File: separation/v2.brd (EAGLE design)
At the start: 0 parts

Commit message: add mcu
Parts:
- added JP2, JP4: (no value), microbuilder:1X07_OVAL
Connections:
- new net +3V3: JP4.5
- new net A0: JP2.1
- new net A1: JP2.2
- new net A2: JP2.3
- new net A3: JP2.4
- new net GND: JP4.6
- new net MISO: JP4.3
- new net MOSI: JP4.4
- new net RX: JP4.1
- new net SCK: JP4.2
- new net SCL: JP2.6
- new net SDA: JP2.5
- new net TX: JP2.7
- new net VCC: JP4.7
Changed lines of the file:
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@@
 <layer number="23" name="tOrigins" color="15" fill="1" visible="yes" active="yes"/>
 <layer number="24" name="bOrigins" color="15" fill="1" visible="yes" active="yes"/>
-<layer number="25" name="tNames" color="7" fill="1" visible="no" active="yes"/>
+<layer number="25" name="tNames" color="7" fill="1" visible="yes" active="yes"/>
 <layer number="26" name="bNames" color="7" fill="1" visible="no" active="yes"/>
 <layer number="27" name="tValues" color="7" fill="1" visible="no" active="yes"/>
 <layer number="28" name="bValues" color="7" fill="1" visible="no" active="yes"/>
-<layer number="29" name="tStop" color="7" fill="3" visible="no" active="yes"/>
+<layer number="29" name="tStop" color="7" fill="3" visible="yes" active="yes"/>
 <layer number="30" name="bStop" color="7" fill="6" visible="no" active="yes"/>
 <layer number="31" name="tCream" color="7" fill="4" visible="no" active="yes"/>
@@
 <wire x1="30.48" y1="64.897" x2="32.258" y2="64.897" width="1.524" layer="29"/>
 <circle x="0" y="0" radius="38" width="0.254" layer="49"/>
+<wire x1="8.89" y1="32.131" x2="8.89" y2="16.51" width="0.254" layer="21"/>
+<wire x1="8.89" y1="16.51" x2="6.35" y2="13.97" width="0.254" layer="21" curve="-90"/>
+<wire x1="6.35" y1="13.97" x2="-6.35" y2="13.97" width="0.254" layer="21"/>
+<wire x1="-6.35" y1="13.97" x2="-8.89" y2="16.51" width="0.254" layer="21" curve="-90"/>
+<wire x1="-8.89" y1="16.51" x2="-8.89" y2="32.131" width="0.254" layer="21"/>
+<wire x1="-8.89" y1="32.131" x2="-6.35" y2="34.671" width="0.254" layer="21" curve="-90"/>
+<wire x1="-6.35" y1="34.671" x2="6.35" y2="34.671" width="0.254" layer="21"/>
+<wire x1="6.35" y1="34.671" x2="8.89" y2="32.131" width="0.254" layer="21" curve="-90"/>
+<text x="64.4398" y="16.5608" size="1.016" layer="21" font="vector" ratio="12" rot="R180" align="center"></text>
+<wire x1="-7.62" y1="32.004" x2="-9.525" y2="32.004" width="1.524" layer="29"/>
+<wire x1="-7.62" y1="29.337" x2="-9.398" y2="29.337" width="1.524" layer="29"/>
+<wire x1="-7.62" y1="26.797" x2="-7.747" y2="26.924" width="1.524" layer="29"/>
+<wire x1="-7.62" y1="21.844" x2="-7.747" y2="21.717" width="1.524" layer="29"/>
+<wire x1="-7.747" y1="21.717" x2="-9.398" y2="21.717" width="1.524" layer="29"/>
+<wire x1="-7.62" y1="26.797" x2="-9.398" y2="26.797" width="1.524" layer="29"/>
+<wire x1="-7.62" y1="24.257" x2="-9.398" y2="24.257" width="1.524" layer="29"/>
+<wire x1="-7.62" y1="19.177" x2="-9.398" y2="19.177" width="1.524" layer="29"/>
+<wire x1="-7.62" y1="16.637" x2="-9.398" y2="16.637" width="1.524" layer="29"/>
+<wire x1="7.62" y1="31.877" x2="9.398" y2="31.877" width="1.524" layer="29"/>
+<wire x1="7.62" y1="29.337" x2="9.398" y2="29.337" width="1.524" layer="29"/>
+<wire x1="7.62" y1="26.797" x2="9.398" y2="26.797" width="1.524" layer="29"/>
+<wire x1="7.62" y1="24.257" x2="9.398" y2="24.257" width="1.524" layer="29"/>
+<wire x1="7.62" y1="21.717" x2="9.398" y2="21.717" width="1.524" layer="29"/>
+<wire x1="7.62" y1="19.177" x2="9.398" y2="19.177" width="1.524" layer="29"/>
+<wire x1="7.62" y1="16.637" x2="9.398" y2="16.637" width="1.524" layer="29"/>
 </plain>
 <attributes>
@@
 </autorouter>
 <elements>
+<element name="JP2" library="microbuilder" package="1X07_OVAL" value="" x="-7.62" y="24.3205" smashed="yes" rot="R270">
+<attribute name="NAME" x="-5.7912" y="33.2867" size="0.8128" layer="25" ratio="18" rot="R270"/>
+<attribute name="VALUE" x="-10.795" y="33.2105" size="0.4064" layer="27" ratio="10" rot="R270"/>
+</element>
+<element name="JP4" library="microbuilder" package="1X07_OVAL" value="" x="7.62" y="24.3205" smashed="yes" rot="R90">
+<attribute name="NAME" x="5.7912" y="15.3543" size="0.8128" layer="25" ratio="18" rot="R90"/>
+<attribute name="VALUE" x="10.795" y="15.4305" size="0.4064" layer="27" ratio="10" rot="R90"/>
+</element>
 </elements>
 <signals>
@@
 <signal name="PB03/I3/AIN11/SERCOM5.2">
 </signal>
+<signal name="GND" class="1">
+<contactref element="JP4" pad="6"/>
+</signal>
+<signal name="A0">
+<contactref element="JP2" pad="1"/>
+</signal>
+<signal name="A1">
+<contactref element="JP2" pad="2"/>
+</signal>
+<signal name="MOSI">
+<contactref element="JP4" pad="4"/>
+</signal>
+<signal name="MISO">
+<contactref element="JP4" pad="3"/>
+</signal>
+<signal name="SCK">
+<contactref element="JP4" pad="2"/>
+</signal>
+<signal name="A2">
+<contactref element="JP2" pad="3"/>
+</signal>
+<signal name="A3">
+<contactref element="JP2" pad="4"/>
+</signal>
+<signal name="SDA">
+<contactref element="JP2" pad="5"/>
+</signal>
+<signal name="SCL">
+<contactref element="JP2" pad="6"/>
+</signal>
+<signal name="VCC" class="1">
+<contactref element="JP4" pad="7"/>
+</signal>
+<signal name="+3V3">
+<contactref element="JP4" pad="5"/>
+</signal>
+<signal name="PB22/I6/SERCOM5.3">
+</signal>
+<signal name="PB23/I7/SERCOM5.2">
+</signal>
+<signal name="PB03/I3/AIN11/SERCOM5.3">
+</signal>
+<signal name="TX">
+<contactref element="JP2" pad="7"/>
+</signal>
+<signal name="RX">
+<contactref element="JP4" pad="1"/>
+</signal>
 </signals>

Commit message: 9mm buzzer
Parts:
- added LS1: KSTG931AP, SamacSys_Parts:CAPPRD400W70D900H500
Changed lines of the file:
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@@
 <attribute name="VALUE" x="10.795" y="15.4305" size="0.4064" layer="27" ratio="10" rot="R90"/>
+</element>
+<element name="LS1" library="SamacSys_Parts" package="CAPPRD400W70D900H500" package3d_urn="urn:adsk.eagle:package:34276129/2" value="KSTG931AP" x="-33.02" y="-43.18" smashed="yes">
+<attribute name="DESCRIPTION" value="RS PRO 4V Electromagnetic Buzzer, 92dB" x="-33.02" y="-43.18" size="1.778" layer="27" font="vector" ratio="15" display="off"/>
+<attribute name="HEIGHT" value="5mm" x="-33.02" y="-43.18" size="1.778" layer="27" font="vector" ratio="15" display="off"/>
+<attribute name="MANUFACTURER_NAME" value="RS Components" x="-33.02" y="-43.18" size="1.778" layer="27" font="vector" ratio="15" display="off"/>
+<attribute name="MANUFACTURER_PART_NUMBER" value="KSTG931AP" x="-33.02" y="-43.18" size="1.778" layer="27" font="vector" ratio="15" display="off"/>
+<attribute name="NAME" x="-33.02" y="-43.18" size="1.27" layer="25" align="center"/>
+<attribute name="RS_PART_NUMBER" value="" x="-33.02" y="-43.18" size="1.778" layer="27" font="vector" ratio="15" display="off"/>
+<attribute name="RS_PRICE-STOCK" value="" x="-33.02" y="-43.18" size="1.778" layer="27" font="vector" ratio="15" display="off"/>
+<attribute name="VALUE" x="-33.02" y="-43.18" size="1.27" layer="27" align="center"/>
 </element>
 </elements>
@@
 </board>
 </drawing>
+<compatibility>
+<note version="8.3" severity="warning">
+Since Version 8.3, EAGLE supports URNs for individual library
+assets (packages, symbols, and devices). The URNs of those assets
+will not be understood (or retained) with this version.
+</note>
+<note version="8.3" severity="warning">
+Since Version 8.3, EAGLE supports the association of 3D packages
+with devices in libraries, schematics, and board files. Those 3D
+packages will not be understood (or retained) with this version.
+</note>
+</compatibility>
 </eagle>

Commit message: add support components
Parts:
- added BAT: MB332-350M02SZ, SamacSys_Parts:MB332350M02SZ
- added LDO: L7805ACV, SamacSys_Parts:TO255P460X1020X2008-3P
- renumbered LS1 to LOUD
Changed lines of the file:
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@@
 <attribute name="VALUE" x="10.795" y="15.4305" size="0.4064" layer="27" ratio="10" rot="R90"/>
 </element>
-<element name="LS1" library="SamacSys_Parts" package="CAPPRD400W70D900H500" package3d_urn="urn:adsk.eagle:package:34276129/2" value="KSTG931AP" x="-33.02" y="-43.18" smashed="yes">
+<element name="LOUD" library="SamacSys_Parts" package="CAPPRD400W70D900H500" package3d_urn="urn:adsk.eagle:package:34276129/2" value="KSTG931AP" x="-33.02" y="-43.18" smashed="yes">
 <attribute name="DESCRIPTION" value="RS PRO 4V Electromagnetic Buzzer, 92dB" x="-33.02" y="-43.18" size="1.778" layer="27" font="vector" ratio="15" display="off"/>
 <attribute name="HEIGHT" value="5mm" x="-33.02" y="-43.18" size="1.778" layer="27" font="vector" ratio="15" display="off"/>
@@
 <attribute name="VALUE" x="-33.02" y="-43.18" size="1.27" layer="27" align="center"/>
 </element>
+<element name="LDO" library="SamacSys_Parts" package="TO255P460X1020X2008-3P" package3d_urn="urn:adsk.eagle:package:34276127/2" value="L7805ACV" x="-34.29" y="-52.07" smashed="yes">
+<attribute name="ALLIED_NUMBER" value="70013701" x="-34.29" y="-52.07" size="1.778" layer="27" font="vector" ratio="15" display="off"/>
+<attribute name="DESCRIPTION" value="Linear voltage regulator,L7805ACV 5V 1A STMicroelectronics L7805ACV, Single Linear Voltage Regulator, 1A 5 V, 2%, 3-Pin TO-220" x="-34.29" y="-52.07" size="1.778" layer="27" font="vector" ratio="15" display="off"/>
+<attribute name="HEIGHT" value="4.6mm" x="-34.29" y="-52.07" size="1.778" layer="27" font="vector" ratio="15" display="off"/>
+<attribute name="MANUFACTURER_NAME" value="STMicroelectronics" x="-34.29" y="-52.07" size="1.778" layer="27" font="vector" ratio="15" display="off"/>
+<attribute name="MANUFACTURER_PART_NUMBER" value="L7805ACV" x="-34.29" y="-52.07" size="1.778" layer="27" font="vector" ratio="15" display="off"/>
+<attribute name="NAME" x="-34.29" y="-52.07" size="1.27" layer="25" align="center"/>
+<attribute name="RS_PART_NUMBER" value="2988508P" x="-34.29" y="-52.07" size="1.778" layer="27" font="vector" ratio="15" display="off"/>
+<attribute name="RS_PRICE-STOCK" value="http://uk.rs-online.com/web/p/products/2988508P" x="-34.29" y="-52.07" size="1.778" layer="27" font="vector" ratio="15" display="off"/>
+<attribute name="VALUE" x="-34.29" y="-52.07" size="1.27" layer="27" align="center"/>
+</element>
+<element name="BAT" library="SamacSys_Parts" package="MB332350M02SZ" value="MB332-350M02SZ" x="-45.72" y="-48.26" smashed="yes">
+<attribute name="DESCRIPTION" value="RS PRO 3.5mm Pitch Straight, PCB Terminal Block, Through Hole, 2 Way" x="-45.72" y="-48.26" size="1.778" layer="27" font="vector" ratio="15" display="off"/>
+<attribute name="HEIGHT" value="12.76mm" x="-45.72" y="-48.26" size="1.778" layer="27" font="vector" ratio="15" display="off"/>
+<attribute name="MANUFACTURER_NAME" value="RS Components" x="-45.72" y="-48.26" size="1.778" layer="27" font="vector" ratio="15" display="off"/>
+<attribute name="MANUFACTURER_PART_NUMBER" value="MB332-350M02SZ" x="-45.72" y="-48.26" size="1.778" layer="27" font="vector" ratio="15" display="off"/>
+<attribute name="NAME" x="-43.97" y="-48.36" size="1.27" layer="25" align="center"/>
+<attribute name="RS_PART_NUMBER" value="7901149" x="-45.72" y="-48.26" size="1.778" layer="27" font="vector" ratio="15" display="off"/>
+<attribute name="RS_PRICE-STOCK" value="https://uk.rs-online.com/web/p/products/7901149" x="-45.72" y="-48.26" size="1.778" layer="27" font="vector" ratio="15" display="off"/>
+<attribute name="VALUE" x="-43.97" y="-48.36" size="1.27" layer="27" align="center"/>
+</element>
 </elements>

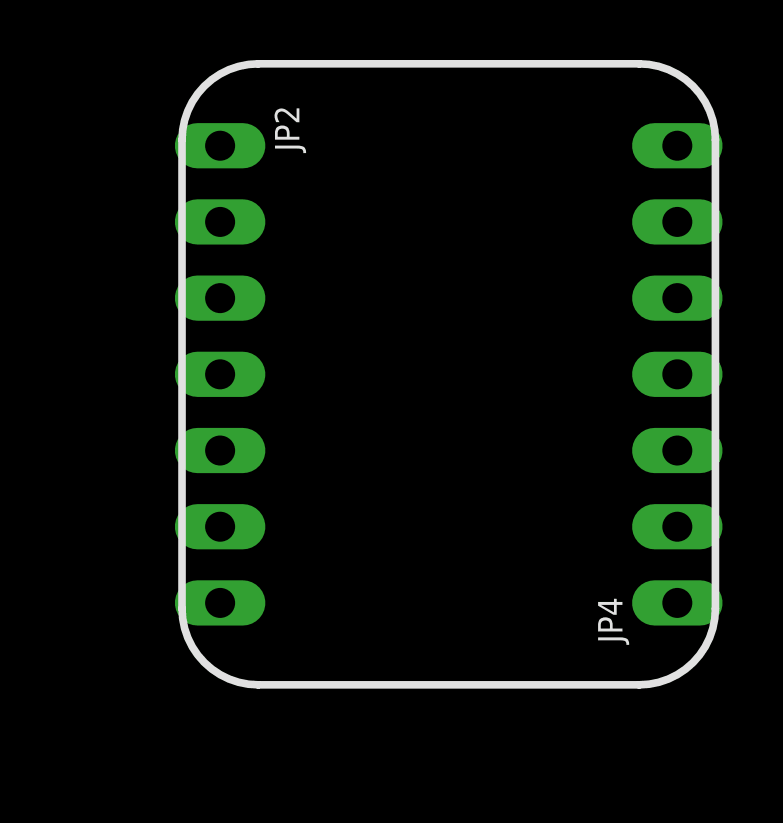
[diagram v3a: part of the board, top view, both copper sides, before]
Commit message: rename components to be helpful
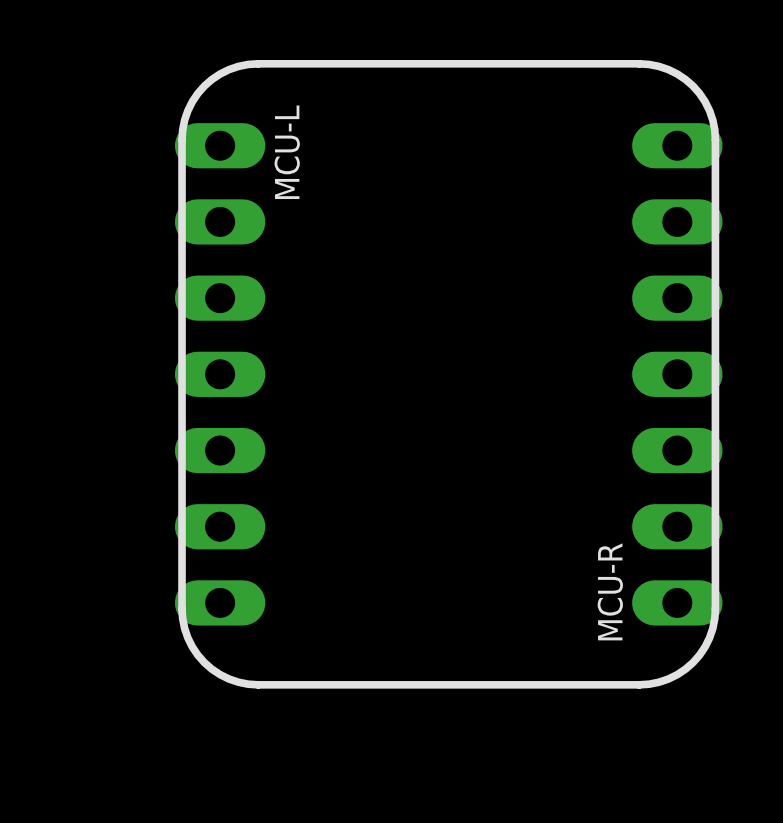
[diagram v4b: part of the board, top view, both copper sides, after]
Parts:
- renumbered JP2 to MCU-L, JP4 to MCU-R
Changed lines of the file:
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@@
 </autorouter>
 <elements>
-<element name="JP2" library="microbuilder" package="1X07_OVAL" value="" x="-7.62" y="24.3205" smashed="yes" rot="R270">
+<element name="MCU-L" library="microbuilder" package="1X07_OVAL" value="" x="-7.62" y="24.3205" smashed="yes" rot="R270">
 <attribute name="NAME" x="-5.7912" y="33.2867" size="0.8128" layer="25" ratio="18" rot="R270"/>
 <attribute name="VALUE" x="-10.795" y="33.2105" size="0.4064" layer="27" ratio="10" rot="R270"/>
 </element>
-<element name="JP4" library="microbuilder" package="1X07_OVAL" value="" x="7.62" y="24.3205" smashed="yes" rot="R90">
+<element name="MCU-R" library="microbuilder" package="1X07_OVAL" value="" x="7.62" y="24.3205" smashed="yes" rot="R90">
 <attribute name="NAME" x="5.7912" y="15.3543" size="0.8128" layer="25" ratio="18" rot="R90"/>
 <attribute name="VALUE" x="10.795" y="15.4305" size="0.4064" layer="27" ratio="10" rot="R90"/>
@@
 </signal>
 <signal name="GND" class="1">
-<contactref element="JP4" pad="6"/>
+<contactref element="MCU-R" pad="6"/>
 </signal>
 <signal name="A0">
-<contactref element="JP2" pad="1"/>
+<contactref element="MCU-L" pad="1"/>
 </signal>
 <signal name="A1">
-<contactref element="JP2" pad="2"/>
+<contactref element="MCU-L" pad="2"/>
 </signal>
 <signal name="MOSI">
-<contactref element="JP4" pad="4"/>
+<contactref element="MCU-R" pad="4"/>
 </signal>
 <signal name="MISO">
-<contactref element="JP4" pad="3"/>
+<contactref element="MCU-R" pad="3"/>
 </signal>
 <signal name="SCK">
-<contactref element="JP4" pad="2"/>
+<contactref element="MCU-R" pad="2"/>
 </signal>
 <signal name="A2">
-<contactref element="JP2" pad="3"/>
+<contactref element="MCU-L" pad="3"/>
 </signal>
 <signal name="A3">
-<contactref element="JP2" pad="4"/>
+<contactref element="MCU-L" pad="4"/>
 </signal>
 <signal name="SDA">
-<contactref element="JP2" pad="5"/>
+<contactref element="MCU-L" pad="5"/>
 </signal>
 <signal name="SCL">
-<contactref element="JP2" pad="6"/>
+<contactref element="MCU-L" pad="6"/>
 </signal>
 <signal name="VCC" class="1">
-<contactref element="JP4" pad="7"/>
+<contactref element="MCU-R" pad="7"/>
 </signal>
 <signal name="+3V3">
-<contactref element="JP4" pad="5"/>
+<contactref element="MCU-R" pad="5"/>
 </signal>
 <signal name="PB22/I6/SERCOM5.3">
@@
 </signal>
 <signal name="TX">
-<contactref element="JP2" pad="7"/>
+<contactref element="MCU-L" pad="7"/>
 </signal>
 <signal name="RX">
-<contactref element="JP4" pad="1"/>
+<contactref element="MCU-R" pad="1"/>
 </signal>
 </signals>

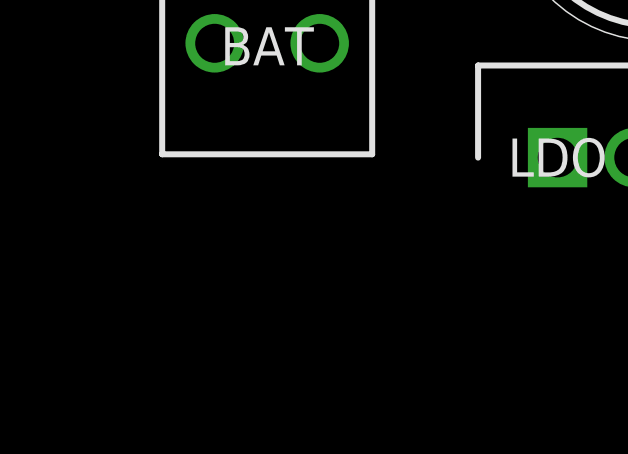
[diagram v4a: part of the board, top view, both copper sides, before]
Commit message: servo connection
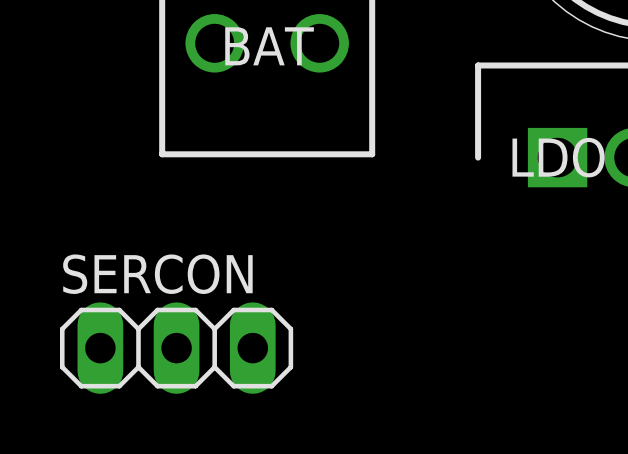
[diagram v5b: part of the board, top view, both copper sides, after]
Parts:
- added SERCON: (no value), pinhead:1X03
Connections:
- new net SERVO: SERCON.3
- new net VBAT: SERCON.1
- net GND: now also SERCON.2
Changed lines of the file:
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@@
 <attribute name="VALUE" x="-43.97" y="-48.36" size="1.27" layer="27" align="center"/>
+</element>
+<element name="SERCON" library="pinhead" library_urn="urn:adsk.eagle:library:325" package="1X03" package3d_urn="urn:adsk.eagle:package:22458/2" value="" x="-46.99" y="-58.42" smashed="yes">
+<attribute name="NAME" x="-50.8762" y="-56.5912" size="1.27" layer="25" ratio="10"/>
+<attribute name="POPULARITY" value="92" x="-46.99" y="-58.42" size="1.778" layer="27" font="vector" ratio="15" display="off"/>
+<attribute name="VALUE" x="-50.8" y="-61.595" size="1.27" layer="27"/>
 </element>
 </elements>
@@
 <signal name="GND" class="1">
 <contactref element="MCU-R" pad="6"/>
+<contactref element="SERCON" pad="2"/>
+<wire x1="7.62" y1="29.4005" x2="-46.99" y2="-58.42" width="0" layer="19" extent="1-1"/>
 </signal>
 <signal name="A0">
@@
 <contactref element="MCU-R" pad="1"/>
 </signal>
+<signal name="VBAT">
+<contactref element="SERCON" pad="1"/>
+</signal>
+<signal name="SERVO">
+<contactref element="SERCON" pad="3"/>
+</signal>
 </signals>
 <mfgpreviewcolors>
@@
 </drawing>
 <compatibility>
+<note version="8.2" severity="warning">
+Since Version 8.2, EAGLE supports online libraries. The ids
+of those online libraries will not be understood (or retained)
+with this version.
+</note>
 <note version="8.3" severity="warning">
 Since Version 8.3, EAGLE supports URNs for individual library

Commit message: ground components
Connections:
- net GND: now also BAT.2, LDO.2, LOUD.2
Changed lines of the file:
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@@
 <contactref element="MCU-R" pad="6"/>
 <contactref element="SERCON" pad="2"/>
-<wire x1="7.62" y1="29.4005" x2="-46.99" y2="-58.42" width="0" layer="19" extent="1-1"/>
+<contactref element="BAT" pad="2"/>
+<contactref element="LDO" pad="2"/>
+<contactref element="LOUD" pad="2"/>
+<wire x1="-42.22" y1="-48.26" x2="-46.99" y2="-58.42" width="0" layer="19" extent="1-1"/>
+<wire x1="-31.74" y1="-52.07" x2="-42.22" y2="-48.26" width="0" layer="19" extent="1-1"/>
+<wire x1="-29.02" y1="-43.18" x2="-31.74" y2="-52.07" width="0" layer="19" extent="1-1"/>
+<wire x1="7.62" y1="29.4005" x2="-29.02" y2="-43.18" width="0" layer="19" extent="1-1"/>
 </signal>
 <signal name="A0">

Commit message: connect components to nets
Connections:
- new net BUZZ: LOUD.1
- net VBAT: now also BAT.1, LDO.1
- net VCC: now also LDO.3
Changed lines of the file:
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@@
 <signal name="VCC" class="1">
 <contactref element="MCU-R" pad="7"/>
+<contactref element="LDO" pad="3"/>
+<wire x1="7.62" y1="31.9405" x2="-29.19" y2="-52.07" width="0" layer="19" extent="1-1"/>
 </signal>
 <signal name="+3V3">
@@
 <signal name="VBAT">
 <contactref element="SERCON" pad="1"/>
+<contactref element="BAT" pad="1"/>
+<contactref element="LDO" pad="1"/>
+<wire x1="-45.72" y1="-48.26" x2="-49.53" y2="-58.42" width="0" layer="19" extent="1-1"/>
+<wire x1="-34.29" y1="-52.07" x2="-45.72" y2="-48.26" width="0" layer="19" extent="1-1"/>
 </signal>
 <signal name="SERVO">
 <contactref element="SERCON" pad="3"/>
 </signal>
+<signal name="BUZZ">
+<contactref element="LOUD" pad="1"/>
+</signal>
 </signals>
